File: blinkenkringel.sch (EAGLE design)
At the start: 85 parts, among them Q1 IRLML2502, Q2 BC337-40, Q3 BC337-40, Q4 BC337-40, Q5 BC337-40

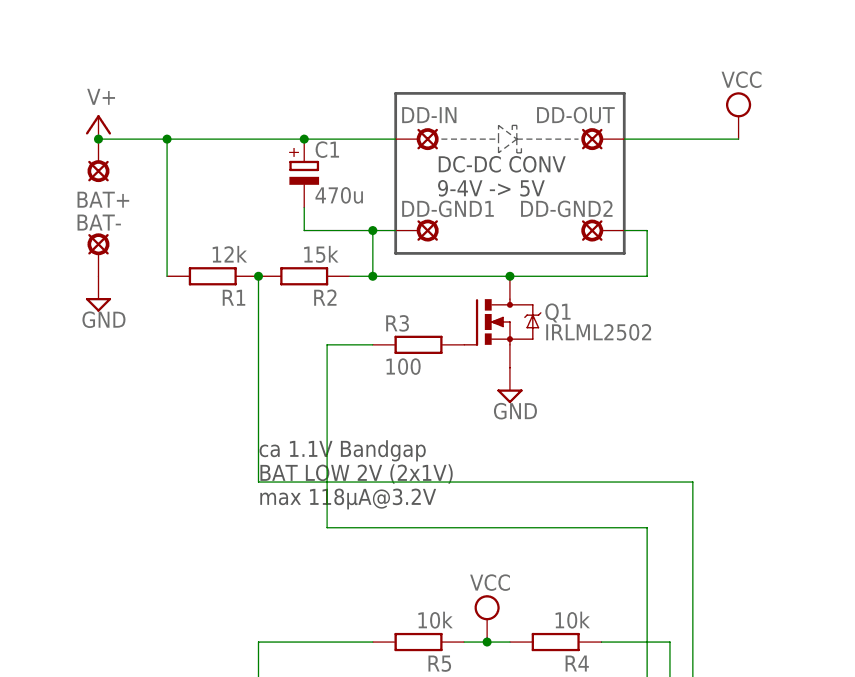
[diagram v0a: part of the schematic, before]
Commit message: changed comparator in for better noise filtering
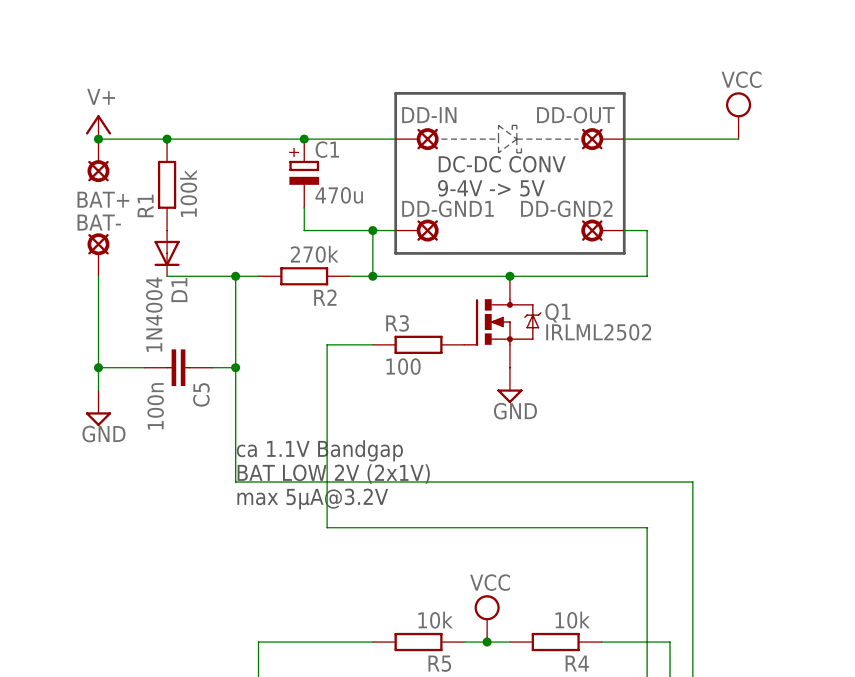
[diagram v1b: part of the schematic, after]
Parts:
- added C5: 100n, rcl:C-EU025-024X044
- added D1: 1N4004, diode:1N4004
- R1: value 12k -> 100k
- R2: value 15k -> 270k
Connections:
- new net N$51: D1.A, R1.1
- net GND: now also C5.2
- net N$4: now also C5.1, D1.C; no longer R1.1
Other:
- note added: "ca 1.1V Bandgap BAT LOW 2V (2x1V) max 5µA@3.2V"
- note removed: "ca 1.1V Bandgap BAT LOW 2V (2x1V) max 118µA@3.2V"
- moved on the sheet: R1
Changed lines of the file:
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@@
 <part name="BAT+" library="solpad" deviceset="MCS10B" device=""/>
 <part name="BAT-" library="solpad" deviceset="MCS10B" device=""/>
-<part name="R1" library="rcl" deviceset="R-EU_" device="0207/7" value="12k"/>
-<part name="R2" library="rcl" deviceset="R-EU_" device="0207/7" value="15k"/>
+<part name="R1" library="rcl" deviceset="R-EU_" device="0207/7" value="100k"/>
+<part name="R2" library="rcl" deviceset="R-EU_" device="0207/7" value="270k"/>
 <part name="C1" library="rcl" deviceset="CPOL-EU" device="E5-8.5" value="470u"/>
 <part name="C2" library="rcl" deviceset="CPOL-EU" device="E5-8.5" value="470u"/>
@@
 <part name="C4" library="rcl" deviceset="C-EU" device="025-024X044" value="100n"/>
 <part name="SUPPLY18" library="supply2" deviceset="GND" device=""/>
+<part name="D1" library="diode" deviceset="1N4004" device=""/>
+<part name="C5" library="rcl" deviceset="C-EU" device="025-024X044" value="100n"/>
 </parts>
 <sheets>
 <sheet>
 <plain>
-<text x="30.48" y="119.38" size="1.778" layer="97">ca 1.1V Bandgap
+<text x="27.94" y="119.38" size="1.778" layer="97">ca 1.1V Bandgap
 BAT LOW 2V (2x1V)
-max 118µA@3.2V</text>
+max 5µA@3.2V</text>
 <wire x1="45.72" y1="165.1" x2="45.72" y2="147.32" width="0.3048" layer="97"/>
 <wire x1="45.72" y1="147.32" x2="71.12" y2="147.32" width="0.3048" layer="97"/>
@@
 <attribute name="NAME" x="10.16" y="149.86" size="1.778" layer="95"/>
 </instance>
-<instance part="R1" gate="G$1" x="25.4" y="144.78" rot="R180"/>
+<instance part="R1" gate="G$1" x="20.32" y="154.94" rot="R90"/>
 <instance part="R2" gate="G$1" x="35.56" y="144.78" rot="R180"/>
 <instance part="C1" gate="G$1" x="35.56" y="157.48"/>
@@
 <instance part="SUPPLY1" gate="G$1" x="55.88" y="106.68"/>
 <instance part="SUPPLY4" gate="GND" x="15.24" y="43.18"/>
-<instance part="SUPPLY5" gate="GND" x="12.7" y="142.24"/>
+<instance part="SUPPLY5" gate="GND" x="12.7" y="129.54"/>
 <instance part="SUPPLY6" gate="GND" x="58.42" y="132.08"/>
 <instance part="SUPPLY3" gate="1" x="12.7" y="162.56"/>
@@
 <instance part="C4" gate="G$1" x="30.48" y="88.9"/>
 <instance part="SUPPLY18" gate="GND" x="30.48" y="81.28"/>
+<instance part="D1" gate="1" x="20.32" y="147.32" rot="R270"/>
+<instance part="C5" gate="G$1" x="22.86" y="134.62" rot="R270"/>
 </instances>
 <busses>
@@
 <net name="N$4" class="0">
 <segment>
-<pinref part="R1" gate="G$1" pin="1"/>
-<pinref part="R2" gate="G$1" pin="2"/>
 <pinref part="U$1" gate="G$1" pin="(AIN0)PB0"/>
 <wire x1="71.12" y1="71.12" x2="78.74" y2="71.12" width="0.1524" layer="91"/>
 <wire x1="78.74" y1="71.12" x2="78.74" y2="121.92" width="0.1524" layer="91"/>
-<wire x1="78.74" y1="121.92" x2="30.48" y2="121.92" width="0.1524" layer="91"/>
-<wire x1="30.48" y1="121.92" x2="30.48" y2="144.78" width="0.1524" layer="91"/>
-<junction x="30.48" y="144.78"/>
+<wire x1="78.74" y1="121.92" x2="27.94" y2="121.92" width="0.1524" layer="91"/>
+<pinref part="D1" gate="1" pin="C"/>
+<pinref part="R2" gate="G$1" pin="2"/>
+<wire x1="20.32" y1="144.78" x2="27.94" y2="144.78" width="0.1524" layer="91"/>
+<wire x1="27.94" y1="144.78" x2="30.48" y2="144.78" width="0.1524" layer="91"/>
+<wire x1="27.94" y1="121.92" x2="27.94" y2="134.62" width="0.1524" layer="91"/>
+<junction x="27.94" y="144.78"/>
+<pinref part="C5" gate="G$1" pin="1"/>
+<wire x1="27.94" y1="134.62" x2="27.94" y2="144.78" width="0.1524" layer="91"/>
+<wire x1="25.4" y1="134.62" x2="27.94" y2="134.62" width="0.1524" layer="91"/>
+<junction x="27.94" y="134.62"/>
 </segment>
 </net>
@@
 <pinref part="BAT-" gate="1" pin="MP"/>
 <pinref part="SUPPLY5" gate="GND" pin="GND"/>
+<wire x1="12.7" y1="132.08" x2="12.7" y2="134.62" width="0.1524" layer="91"/>
+<wire x1="12.7" y1="134.62" x2="12.7" y2="144.78" width="0.1524" layer="91"/>
+<wire x1="12.7" y1="134.62" x2="17.78" y2="134.62" width="0.1524" layer="91"/>
+<junction x="12.7" y="134.62"/>
+<pinref part="C5" gate="G$1" pin="2"/>
 </segment>
 <segment>
@@
 <pinref part="R1" gate="G$1" pin="2"/>
 <wire x1="20.32" y1="160.02" x2="35.56" y2="160.02" width="0.1524" layer="91"/>
-<wire x1="20.32" y1="144.78" x2="20.32" y2="160.02" width="0.1524" layer="91"/>
 <junction x="20.32" y="160.02"/>
 </segment>
@@
 </segment>
 </net>
+<net name="N$51" class="0">
+<segment>
+<pinref part="R1" gate="G$1" pin="1"/>
+<pinref part="D1" gate="1" pin="A"/>
+</segment>
+</net>

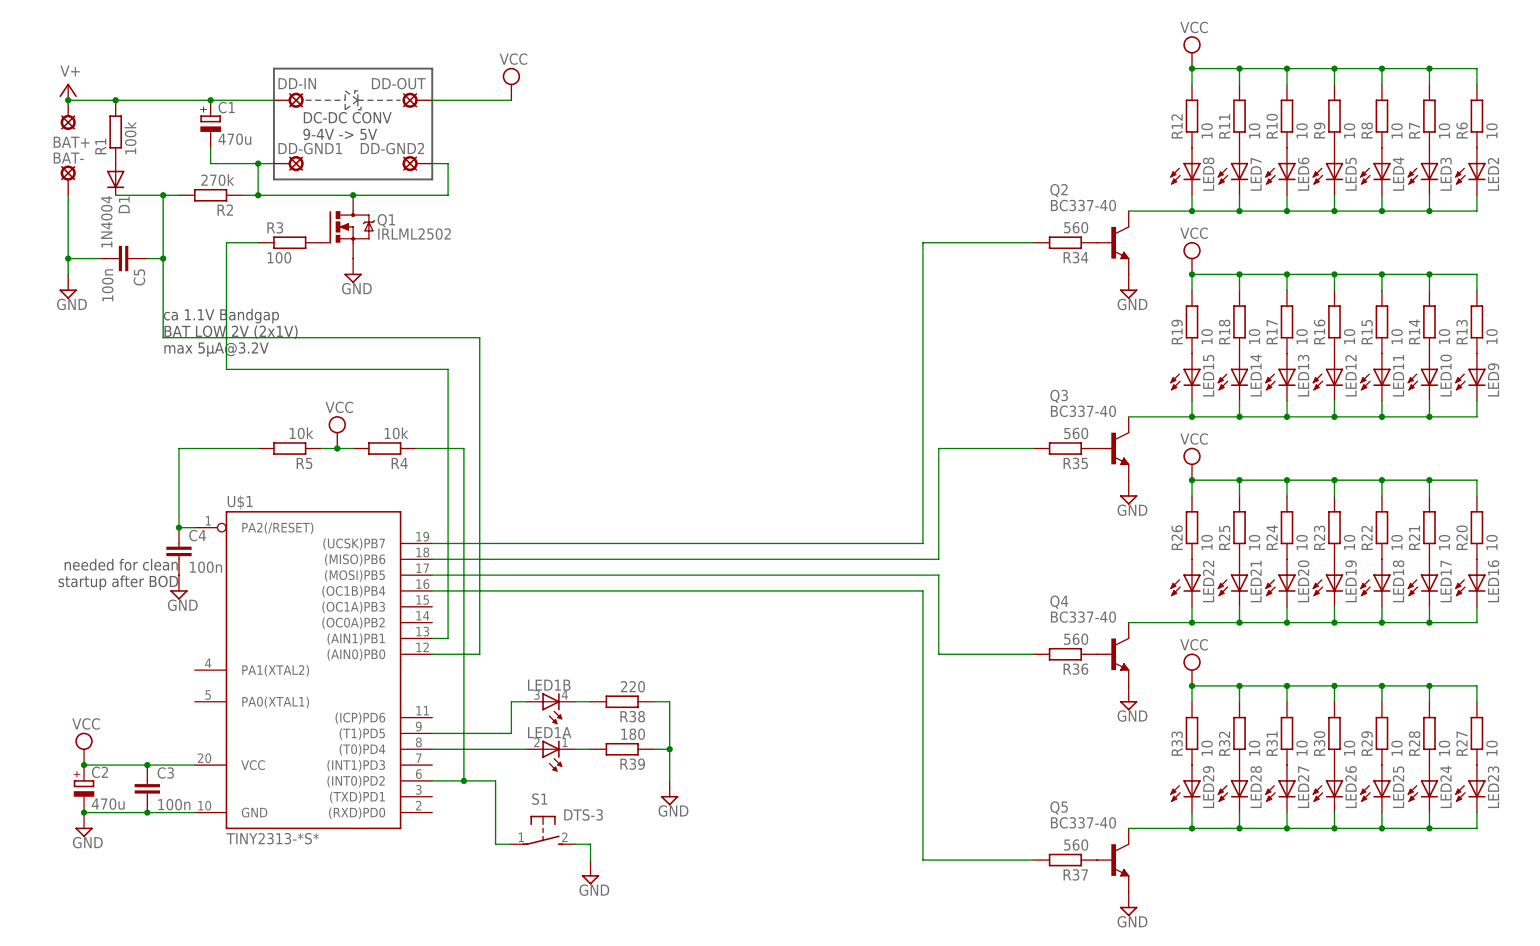
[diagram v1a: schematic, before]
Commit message: free successive pins, uc directly on bats
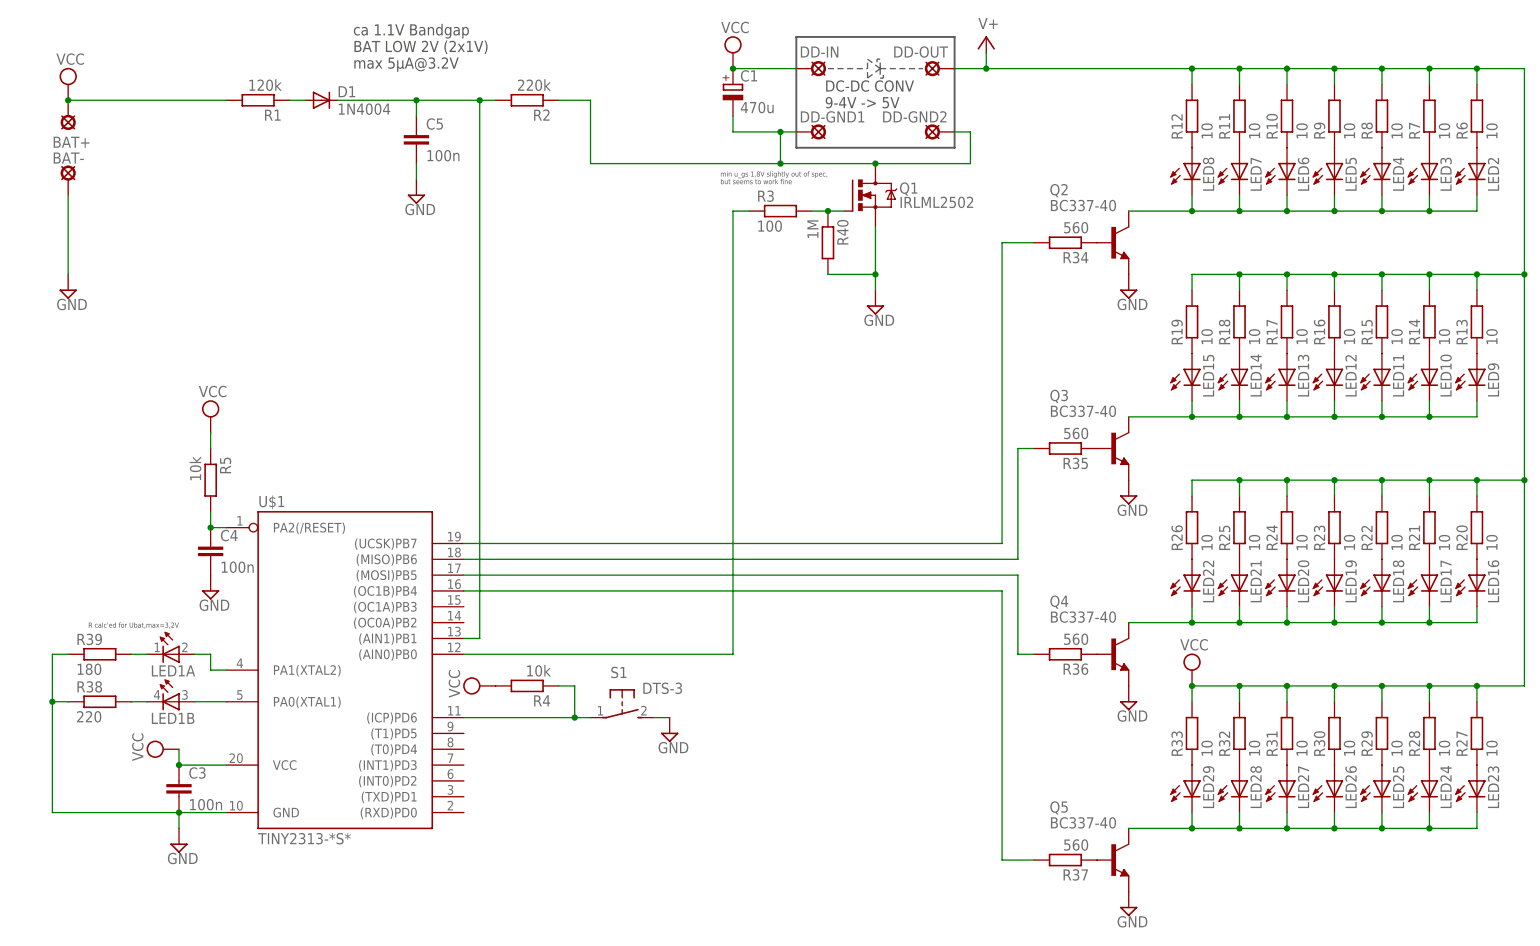
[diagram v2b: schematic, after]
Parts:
- removed C2: 470u, rcl:CPOL-EUE5-8.5
- added R40: 1M, rcl:R-EU_0207/7
- R1: value 100k -> 120k
- R2: value 270k -> 220k
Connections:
- net GND: now also R40.2; no longer C2.-
- net N$4: now also U$1.(AIN1)PB1; no longer U$1.(AIN0)PB0
- net N$44: now also LED1B.A, U$1.PA0(XTAL1); no longer LED1A.A, U$1.(T0)PD4
- net N$45: now also LED1A.A, U$1.PA1(XTAL2); no longer LED1B.A, U$1.(T1)PD5
- net N$46: now also U$1.(ICP)PD6; no longer U$1.(INT0)PD2
- net N$47: now also U$1.(AIN0)PB0; no longer U$1.(AIN1)PB1
- net N$6: now also R40.1
- net V+: now also DD-OUT.MP, R10.2, R11.2, R12.2, R13.2, R14.2, R15.2, R16.2, R17.2, R18.2, R19.2, R20.2, R21.2, R22.2, R23.2, R24.2, R25.2, R26.2, R27.2, R28.2, R29.2, R30.2, R31.2, R32.2, R33.2, R6.2, R7.2, R8.2, R9.2; no longer BAT+.MP, C1.+, DD-IN.MP, R1.2
- net VCC: now also BAT+.MP, C1.+, DD-IN.MP, R1.2; no longer C2.+, DD-OUT.MP, R10.2, R11.2, R12.2, R13.2, R14.2, R15.2, R16.2, R17.2, R18.2, R19.2, R20.2, R21.2, R22.2, R23.2, R24.2, R25.2, R26.2, R27.2, R28.2, R29.2, R30.2, R31.2, R32.2, R33.2, R6.2, R7.2, R8.2, R9.2
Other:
- note added: "R calc'ed for Ubat,max=3,2V"
- note added: "min u_gs 1,8V slightly out of spec, but seems to work fine"
- note removed: "needed for clean startup after BOD"
- moved on the sheet: C1, C3, C4, C5, D1, DD-GND1, DD-GND2, DD-IN, DD-OUT, LED1A, LED1B, Q1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

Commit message: matching schematics and reality: pot for low bat voltage
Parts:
- added R41: 10k, pot:TRIM_EU-CA9V
- R1: value 120k -> 100k
- R2: value 220k -> 150k
- R38: value 220 -> 82
- R39: value 180 -> 56
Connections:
- new net N$52: D1.A, R41.S
- net N$51: now also R41.A; no longer D1.A
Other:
- note added: "grün"
- note added: "rot"
- moved on the sheet: R1
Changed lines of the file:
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@@
 <part name="BAT+" library="solpad" deviceset="MCS10B" device=""/>
 <part name="BAT-" library="solpad" deviceset="MCS10B" device=""/>
-<part name="R1" library="rcl" deviceset="R-EU_" device="0207/7" value="120k"/>
-<part name="R2" library="rcl" deviceset="R-EU_" device="0207/7" value="220k"/>
+<part name="R1" library="rcl" deviceset="R-EU_" device="0207/7" value="100k"/>
+<part name="R2" library="rcl" deviceset="R-EU_" device="0207/7" value="150k"/>
 <part name="C1" library="rcl" deviceset="CPOL-EU" device="E5-8.5" value="470u"/>
 <part name="Q1" library="mosfet" deviceset="IRLML2502" device=""/>
@@
 <part name="R37" library="rcl" deviceset="R-EU_" device="0207/7" value="560"/>
 <part name="SUPPLY15" library="supply2" deviceset="GND" device=""/>
-<part name="R38" library="rcl" deviceset="R-EU_" device="0207/7" value="220"/>
-<part name="R39" library="rcl" deviceset="R-EU_" device="0207/7" value="180"/>
+<part name="R38" library="rcl" deviceset="R-EU_" device="0207/7" value="82"/>
+<part name="R39" library="rcl" deviceset="R-EU_" device="0207/7" value="56"/>
 <part name="S1" library="switch-tact" deviceset="DTS-3" device=""/>
 <part name="SUPPLY17" library="supply2" deviceset="GND" device=""/>
@@
 <part name="SUPPLY10" library="supply2" deviceset="V+" device=""/>
 <part name="R40" library="rcl" deviceset="R-EU_" device="0207/7" value="1M"/>
+<part name="R41" library="pot" deviceset="TRIM_EU-" device="CA9V" value="10k"/>
 </parts>
 <sheets>
@@
 but seems to work fine</text>
 <text x="30.48" y="76.2" size="0.8128" layer="97" rot="R180">R calc'ed for Ubat,max=3,2V</text>
+<text x="7.62" y="71.12" size="1.778" layer="97">grün</text>
+<text x="7.62" y="63.5" size="1.778" layer="97">rot</text>
 </plain>
 <instances>
@@
 <attribute name="NAME" x="10.16" y="149.86" size="1.778" layer="95"/>
 </instance>
-<instance part="R1" gate="G$1" x="43.18" y="160.02" rot="R180"/>
+<instance part="R1" gate="G$1" x="30.48" y="160.02" rot="R180"/>
 <instance part="R2" gate="G$1" x="86.36" y="160.02" rot="R180"/>
 <instance part="C1" gate="G$1" x="119.38" y="162.56"/>
@@
 <instance part="SUPPLY10" gate="1" x="160.02" y="170.18"/>
 <instance part="R40" gate="G$1" x="134.62" y="137.16" rot="R270"/>
+<instance part="R41" gate="1" x="43.18" y="160.02" rot="R270"/>
 </instances>
 <busses>
@@
 <pinref part="R1" gate="G$1" pin="2"/>
 <pinref part="BAT+" gate="1" pin="MP"/>
-<wire x1="12.7" y1="160.02" x2="38.1" y2="160.02" width="0.1524" layer="91"/>
+<wire x1="12.7" y1="160.02" x2="25.4" y2="160.02" width="0.1524" layer="91"/>
 <pinref part="SUPPLY2" gate="G$1" pin="VCC"/>
 <junction x="12.7" y="160.02"/>
@@
 <pinref part="U$1" gate="G$1" pin="(AIN0)PB0"/>
 <wire x1="76.2" y1="71.12" x2="119.38" y2="71.12" width="0.1524" layer="91"/>
-</segment>
-</net>
-<net name="N$51" class="0">
-<segment>
-<pinref part="R1" gate="G$1" pin="1"/>
-<pinref part="D1" gate="1" pin="A"/>
-<wire x1="50.8" y1="160.02" x2="48.26" y2="160.02" width="0.1524" layer="91"/>
 </segment>
 </net>
@@
 </segment>
 </net>
+<net name="N$51" class="0">
+<segment>
+<pinref part="R1" gate="G$1" pin="1"/>
+<pinref part="R41" gate="1" pin="A"/>
+<wire x1="35.56" y1="160.02" x2="38.1" y2="160.02" width="0.1524" layer="91"/>
+</segment>
+</net>
+<net name="N$52" class="0">
+<segment>
+<pinref part="R41" gate="1" pin="S"/>
+<wire x1="43.18" y1="154.94" x2="50.8" y2="154.94" width="0.1524" layer="91"/>
+<pinref part="D1" gate="1" pin="A"/>
+<wire x1="50.8" y1="154.94" x2="50.8" y2="160.02" width="0.1524" layer="91"/>
+</segment>
+</net>

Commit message: misplaced capacitor
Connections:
- net GND: now also C1.-, DD-GND1.MP
- net N$5: no longer C1.-, DD-GND1.MP
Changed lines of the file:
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@@
 <part name="R40" library="rcl" deviceset="R-EU_" device="0207/7" value="1M"/>
 <part name="R41" library="pot" deviceset="TRIM_EU-" device="CA9V" value="10k"/>
+<part name="SUPPLY16" library="supply2" deviceset="GND" device=""/>
 </parts>
 <sheets>
@@
 <instance part="R40" gate="G$1" x="134.62" y="137.16" rot="R270"/>
 <instance part="R41" gate="1" x="43.18" y="160.02" rot="R270"/>
+<instance part="SUPPLY16" gate="GND" x="119.38" y="152.4"/>
 </instances>
 <busses>
@@
 <wire x1="157.48" y1="154.94" x2="157.48" y2="149.86" width="0.1524" layer="91"/>
 <wire x1="157.48" y1="149.86" x2="142.24" y2="149.86" width="0.1524" layer="91"/>
-<wire x1="142.24" y1="149.86" x2="127" y2="149.86" width="0.1524" layer="91"/>
-<wire x1="127" y1="149.86" x2="127" y2="154.94" width="0.1524" layer="91"/>
-<pinref part="DD-GND1" gate="1" pin="MP"/>
-<wire x1="127" y1="154.94" x2="129.54" y2="154.94" width="0.1524" layer="91"/>
-<junction x="127" y="149.86"/>
 <pinref part="R2" gate="G$1" pin="1"/>
 <wire x1="91.44" y1="160.02" x2="96.52" y2="160.02" width="0.1524" layer="91"/>
 <wire x1="96.52" y1="160.02" x2="96.52" y2="149.86" width="0.1524" layer="91"/>
-<wire x1="96.52" y1="149.86" x2="127" y2="149.86" width="0.1524" layer="91"/>
-<wire x1="127" y1="154.94" x2="119.38" y2="154.94" width="0.1524" layer="91"/>
-<junction x="127" y="154.94"/>
-<pinref part="C1" gate="G$1" pin="-"/>
-<wire x1="119.38" y1="154.94" x2="119.38" y2="157.48" width="0.1524" layer="91"/>
+<wire x1="96.52" y1="149.86" x2="142.24" y2="149.86" width="0.1524" layer="91"/>
 <pinref part="Q1" gate="G$1" pin="D"/>
 <junction x="142.24" y="149.86"/>
@@
 <wire x1="68.58" y1="149.86" x2="68.58" y2="147.32" width="0.1524" layer="91"/>
 </segment>
-</net>
+<segment>
+<pinref part="C1" gate="G$1" pin="-"/>
+<pinref part="DD-GND1" gate="1" pin="MP"/>
+<wire x1="129.54" y1="154.94" x2="119.38" y2="154.94" width="0.1524" layer="91"/>
+<wire x1="119.38" y1="154.94" x2="119.38" y2="157.48" width="0.1524" layer="91"/>
+<pinref part="SUPPLY16" gate="GND" pin="GND"/>
+<junction x="119.38" y="154.94"/>
+</segment>
+</net>
